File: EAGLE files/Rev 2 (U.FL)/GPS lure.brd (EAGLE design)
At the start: 35.6 x 27.9 mm, 8 parts, among them J1 U.FL

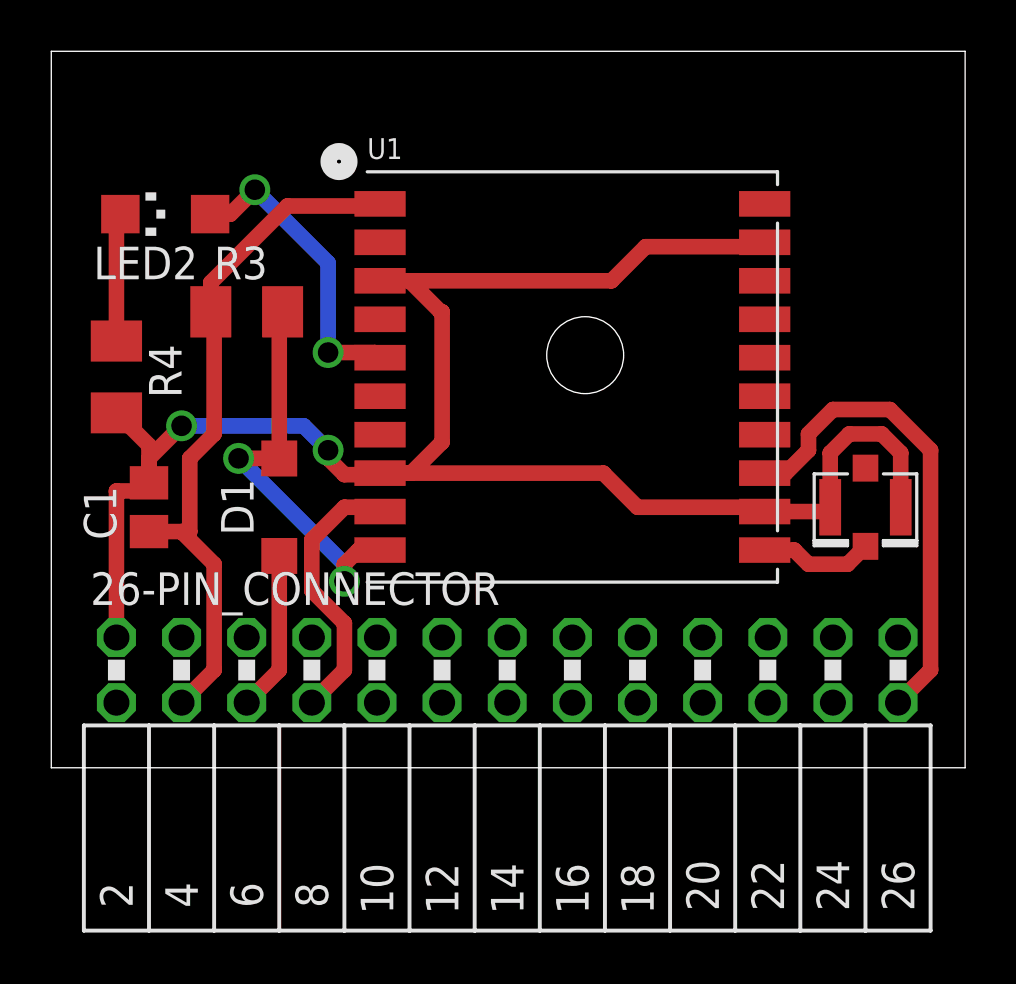
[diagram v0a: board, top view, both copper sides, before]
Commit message: Updated Eagle Files to make silkscreen cleaner
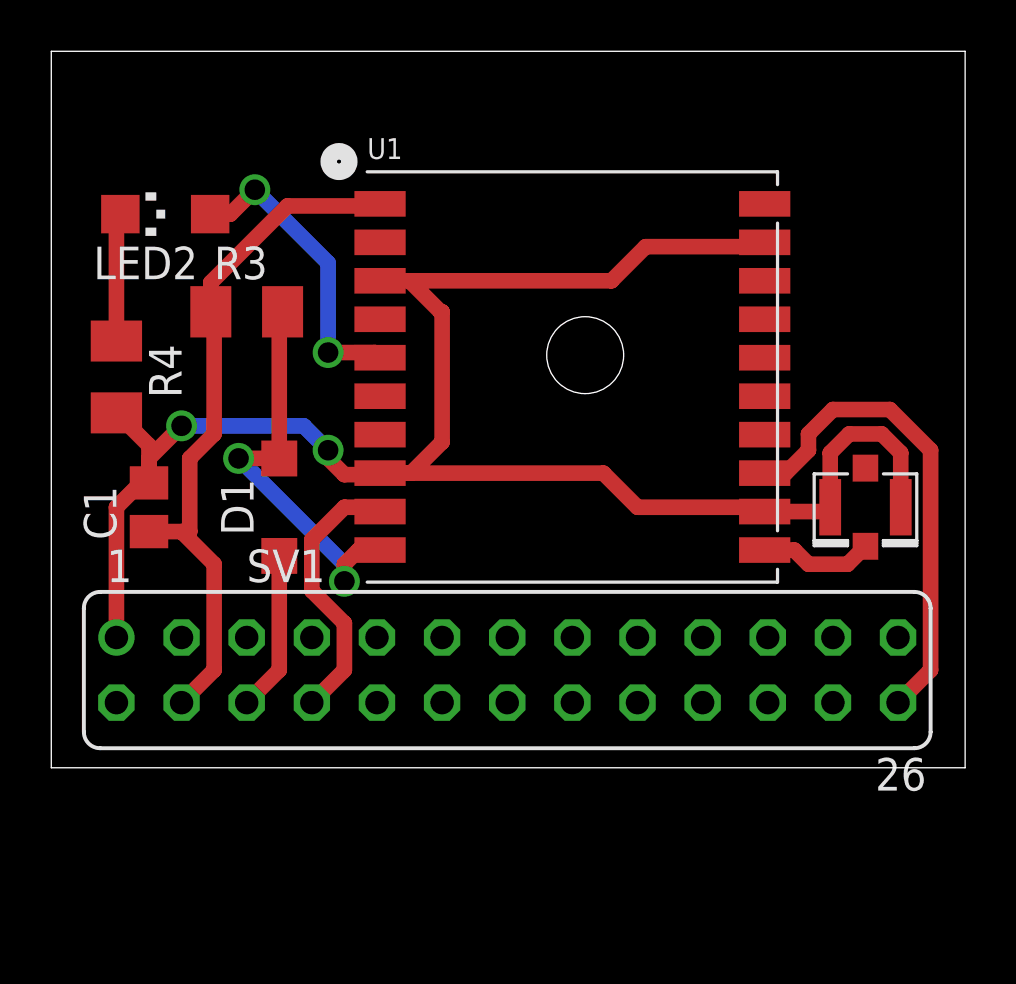
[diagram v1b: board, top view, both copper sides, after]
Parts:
- removed 26-PIN_CONNECTOR: (no value), con-lsta:FE13-2W
- added SV1: (no value), con-lsta:FE13-2
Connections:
- net 3V3: now also SV1.4; no longer 26-PIN_CONNECTOR.4
- net GND: now also SV1.1; no longer 26-PIN_CONNECTOR.1
- net PPS: now also SV1.26; no longer 26-PIN_CONNECTOR.26
- net RX_OUT: now also SV1.6; no longer 26-PIN_CONNECTOR.6
- net TX: now also SV1.8; no longer 26-PIN_CONNECTOR.8
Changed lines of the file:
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@@
 </autorouter>
 <elements>
-<element name="26-PIN_CONNECTOR" library="con-lsta" package="FE13-2W" value="" x="17.78" y="3.81">
-<attribute name="OC_NEWARK" value="unknown" x="17.78" y="3.81" size="1.778" layer="27" display="off"/>
-<attribute name="OC_FARNELL" value="unknown" x="17.78" y="3.81" size="1.778" layer="27" display="off"/>
-<attribute name="MPN" value="" x="17.78" y="3.81" size="1.778" layer="27" display="off"/>
-<attribute name="MF" value="" x="17.78" y="3.81" size="1.778" layer="27" display="off"/>
-</element>
 <element name="U1" library="adafruit" package="FGPMMOPA6H" value="" x="20.32" y="15.24"/>
 <element name="D1" library="diode" package="SOD123" value="1N4148" x="8.89" y="10.16" rot="R90"/>
@@
 <attribute name="PROD_ID" value="CONN-09193" x="31.75" y="10.16" size="1.778" layer="27" rot="R270" display="off"/>
 </element>
+<element name="SV1" library="con-lsta" package="FE13-2" value="" x="17.78" y="3.81">
+<attribute name="OC_NEWARK" value="unknown" x="17.78" y="3.81" size="1.778" layer="27" display="off"/>
+<attribute name="MPN" value="" x="17.78" y="3.81" size="1.778" layer="27" display="off"/>
+<attribute name="MF" value="" x="17.78" y="3.81" size="1.778" layer="27" display="off"/>
+<attribute name="OC_FARNELL" value="unknown" x="17.78" y="3.81" size="1.778" layer="27" display="off"/>
+</element>
 </elements>
 <signals>
 <signal name="GND">
-<contactref element="26-PIN_CONNECTOR" pad="1"/>
 <contactref element="U1" pad="P$3"/>
 <contactref element="U1" pad="P$19"/>
@@
 <contactref element="J1" pad="P$1"/>
 <contactref element="J1" pad="P$2"/>
-<wire x1="2.54" y1="5.08" x2="2.54" y2="10.795" width="0.6096" layer="1"/>
-<wire x1="2.54" y1="10.795" x2="3.495" y2="10.795" width="0.6096" layer="1"/>
 <wire x1="3.495" y1="10.795" x2="3.81" y2="11.11" width="0.6096" layer="1"/>
 <wire x1="3.81" y1="11.11" x2="3.81" y2="12.57" width="0.6096" layer="1"/>
@@
 <wire x1="33.125" y1="12.2775" x2="32.385" y2="13.0175" width="0.6096" layer="1"/>
 <wire x1="32.385" y1="13.0175" x2="31.115" y2="13.0175" width="0.6096" layer="1"/>
+<contactref element="SV1" pad="1"/>
+<wire x1="2.54" y1="5.08" x2="2.54" y2="10.16" width="0.6096" layer="1"/>
+<wire x1="2.54" y1="10.16" x2="3.49" y2="11.11" width="0.6096" layer="1"/>
+<wire x1="3.49" y1="11.11" x2="3.81" y2="11.11" width="0.6096" layer="1"/>
 </signal>
 <signal name="3V3">
-<contactref element="26-PIN_CONNECTOR" pad="4"/>
 <contactref element="U1" pad="P$1"/>
 <contactref element="R3" pad="1"/>
@@
 <wire x1="3.81" y1="9.21" x2="5.08" y2="9.21" width="0.6096" layer="1"/>
 <wire x1="5.08" y1="9.21" x2="5.4" y2="9.21" width="0.6096" layer="1"/>
-<wire x1="5.08" y1="2.54" x2="6.35" y2="3.81" width="0.6096" layer="1"/>
 <wire x1="6.35" y1="3.81" x2="6.35" y2="7.94" width="0.6096" layer="1"/>
 <wire x1="6.35" y1="7.94" x2="5.08" y2="9.21" width="0.6096" layer="1"/>
@@
 <wire x1="6.35" y1="13.0175" x2="6.35" y2="17.65" width="0.6096" layer="1"/>
 <wire x1="6.35" y1="17.65" x2="6.22" y2="17.78" width="0.6096" layer="1"/>
+<contactref element="SV1" pad="4"/>
+<wire x1="6.35" y1="3.81" x2="5.08" y2="2.54" width="0.6096" layer="1"/>
 </signal>
 <signal name="N$1">
@@
 <signal name="PPS">
 <contactref element="U1" pad="P$13"/>
-<contactref element="26-PIN_CONNECTOR" pad="26"/>
 <wire x1="27.82" y1="11.49" x2="28.635" y2="11.49" width="0.6096" layer="1"/>
 <wire x1="28.635" y1="11.49" x2="29.5275" y2="12.3825" width="0.6096" layer="1"/>
@@
 <wire x1="32.7025" y1="13.97" x2="34.29" y2="12.3825" width="0.6096" layer="1"/>
 <wire x1="34.29" y1="12.3825" x2="34.29" y2="3.81" width="0.6096" layer="1"/>
+<contactref element="SV1" pad="26"/>
 <wire x1="34.29" y1="3.81" x2="33.02" y2="2.54" width="0.6096" layer="1"/>
 </signal>
@@
 <wire x1="11.43" y1="10.16" x2="12.65" y2="10.16" width="0.6096" layer="1"/>
 <wire x1="12.65" y1="10.16" x2="12.82" y2="9.99" width="0.6096" layer="1"/>
-<contactref element="26-PIN_CONNECTOR" pad="8"/>
 <wire x1="10.16" y1="8.89" x2="10.16" y2="6.905625" width="0.6096" layer="1"/>
 <wire x1="10.16" y1="6.905625" x2="11.43" y2="5.635625" width="0.6096" layer="1"/>
 <wire x1="11.43" y1="5.635625" x2="11.43" y2="3.81" width="0.6096" layer="1"/>
+<contactref element="SV1" pad="8"/>
 <wire x1="11.43" y1="3.81" x2="10.16" y2="2.54" width="0.6096" layer="1"/>
 </signal>
 <signal name="RX_OUT">
 <contactref element="D1" pad="C"/>
-<contactref element="26-PIN_CONNECTOR" pad="6"/>
-<wire x1="7.62" y1="2.54" x2="8.89" y2="3.81" width="0.6096" layer="1"/>
 <wire x1="8.89" y1="3.81" x2="8.89" y2="8.26" width="0.6096" layer="1"/>
+<contactref element="SV1" pad="6"/>
+<wire x1="8.89" y1="3.81" x2="7.62" y2="2.54" width="0.6096" layer="1"/>
 </signal>
 <signal name="EX_ANT">
